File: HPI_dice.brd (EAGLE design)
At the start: 100 x 80 mm, 35 parts, among them IC1 4017N, IC2 NE555N, T1 BC547, T2 BC557, T3 BC557, T4 BC547, T5 BC547

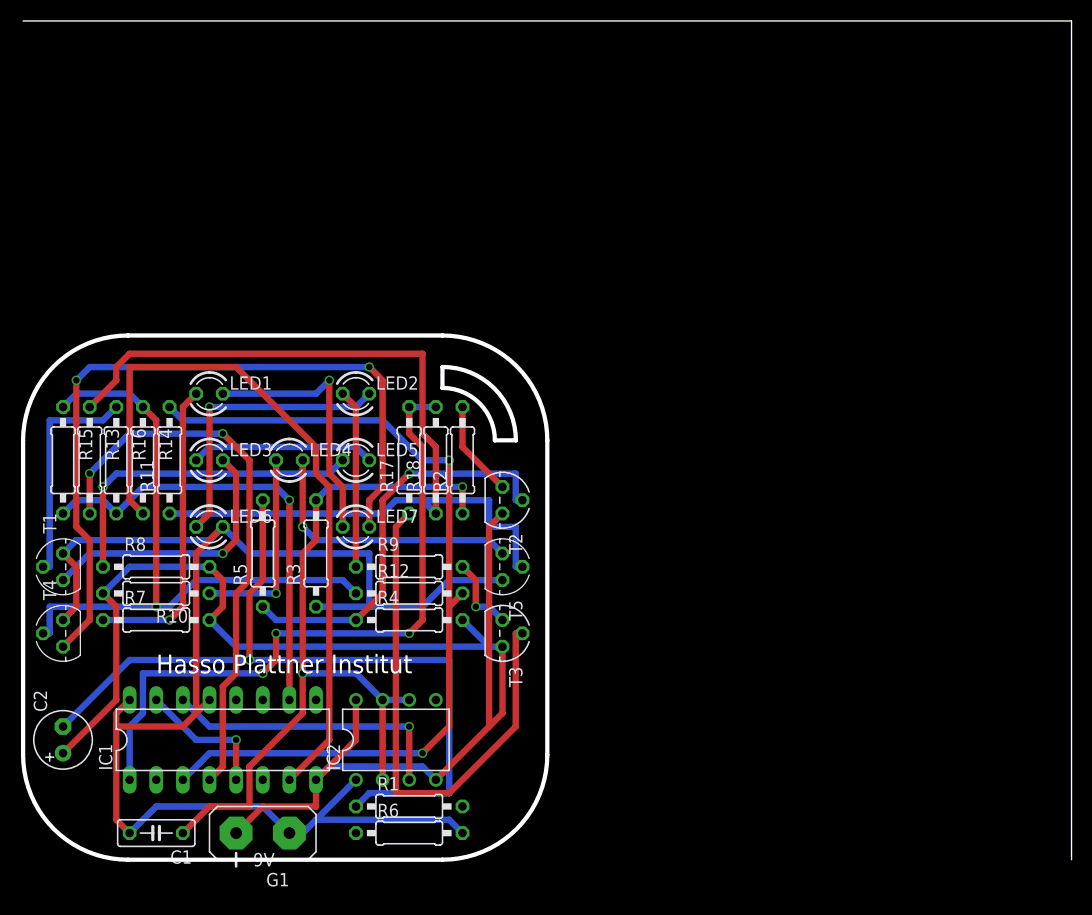
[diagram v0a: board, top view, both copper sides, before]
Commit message: Board layout improvement
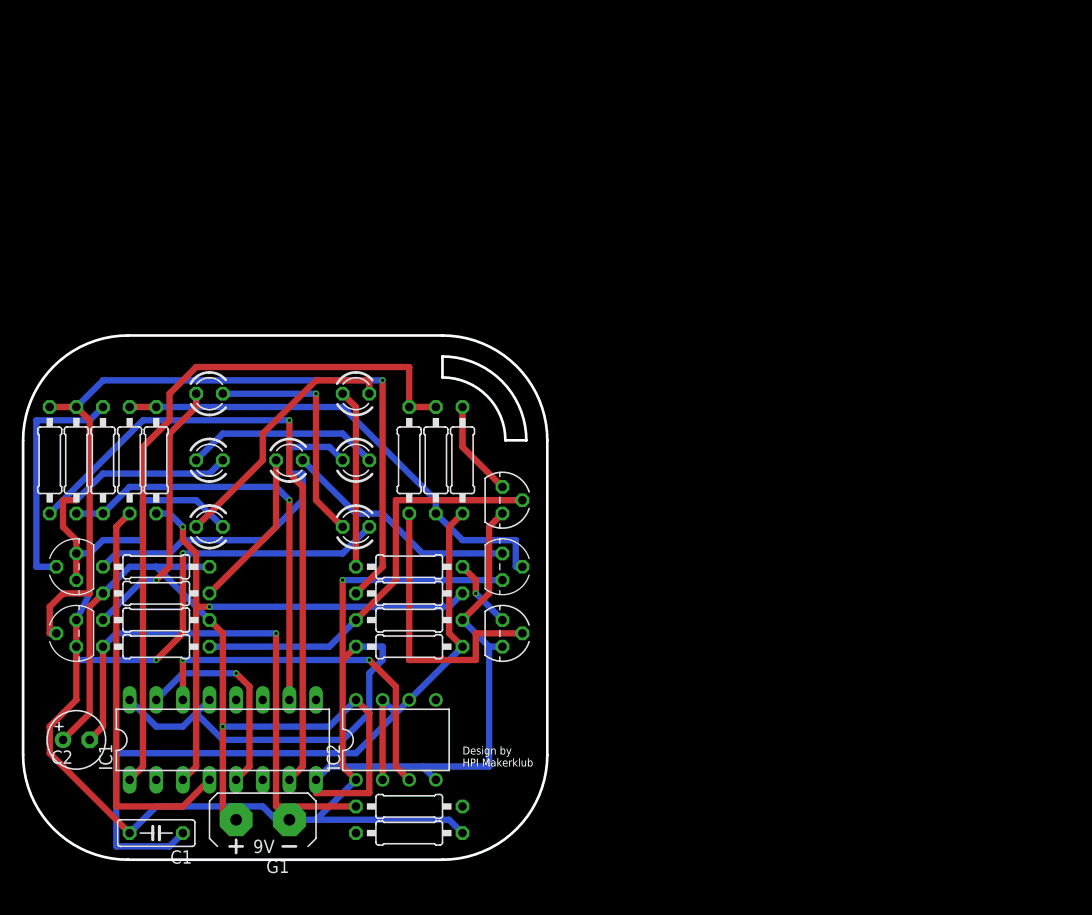
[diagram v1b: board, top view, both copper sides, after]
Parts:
- moved R5 13.5 mm to (12.7, 20.3), turned to 180 degrees
- moved R3 12.6 mm to (36.8, 20.3), turned to 0 degrees
- moved R14 8.89 mm to (2.54, 38.1)
- moved R13 3.81 mm to (10.2, 38.1)
- moved R11 1.27 mm to (12.7, 38.1), turned to 270 degrees
- moved R16 1.27 mm to (7.62, 38.1)
- moved C2 1.27 mm to (5.08, 11.4), turned to 0 degrees
- moved G1 1.27 mm to (22.9, 3.81)
- moved R15 1.27 mm to (5.08, 38.1)
- moved T1 1.27 mm to (5.08, 27.9)
- moved T4 1.27 mm to (5.08, 21.6)
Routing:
- net N$19: track 92.7 -> 46.0 mm
- net N$15: track 71.7 -> 38.9 mm
- net N$18: track 83.5 -> 54.2 mm
- net N$6: track 77.3 -> 50.6 mm
- net N$26: track 50.8 -> 27.3 mm
- net GND: track 145.4 -> 164.1 mm, vias 0 -> 1
- net N$20: track 62.2 -> 80.0 mm
- net N$21: track 53.7 -> 38.4 mm, vias 2 -> 0
- net N$22: track 69.3 -> 61.9 mm, vias 0 -> 1
- net N$1: track 13.0 -> 19.9 mm
- net N$3: track 27.7 -> 34.6 mm, vias 1 -> 2
- net +9V: track 136.9 -> 131.2 mm, vias 0 -> 1
- net N$25: track 64.3 -> 68.7 mm, vias 3 -> 0
- net N$17: track 26.5 -> 22.7 mm, vias 1 -> 0
- net N$16: track 19.1 -> 15.3 mm, vias 1 -> 0
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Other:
- board size 100 x 80 mm -> 50 x 50 mm
- board text added: "Design by HPI Makerklub"
